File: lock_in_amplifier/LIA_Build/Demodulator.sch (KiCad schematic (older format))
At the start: 0 parts

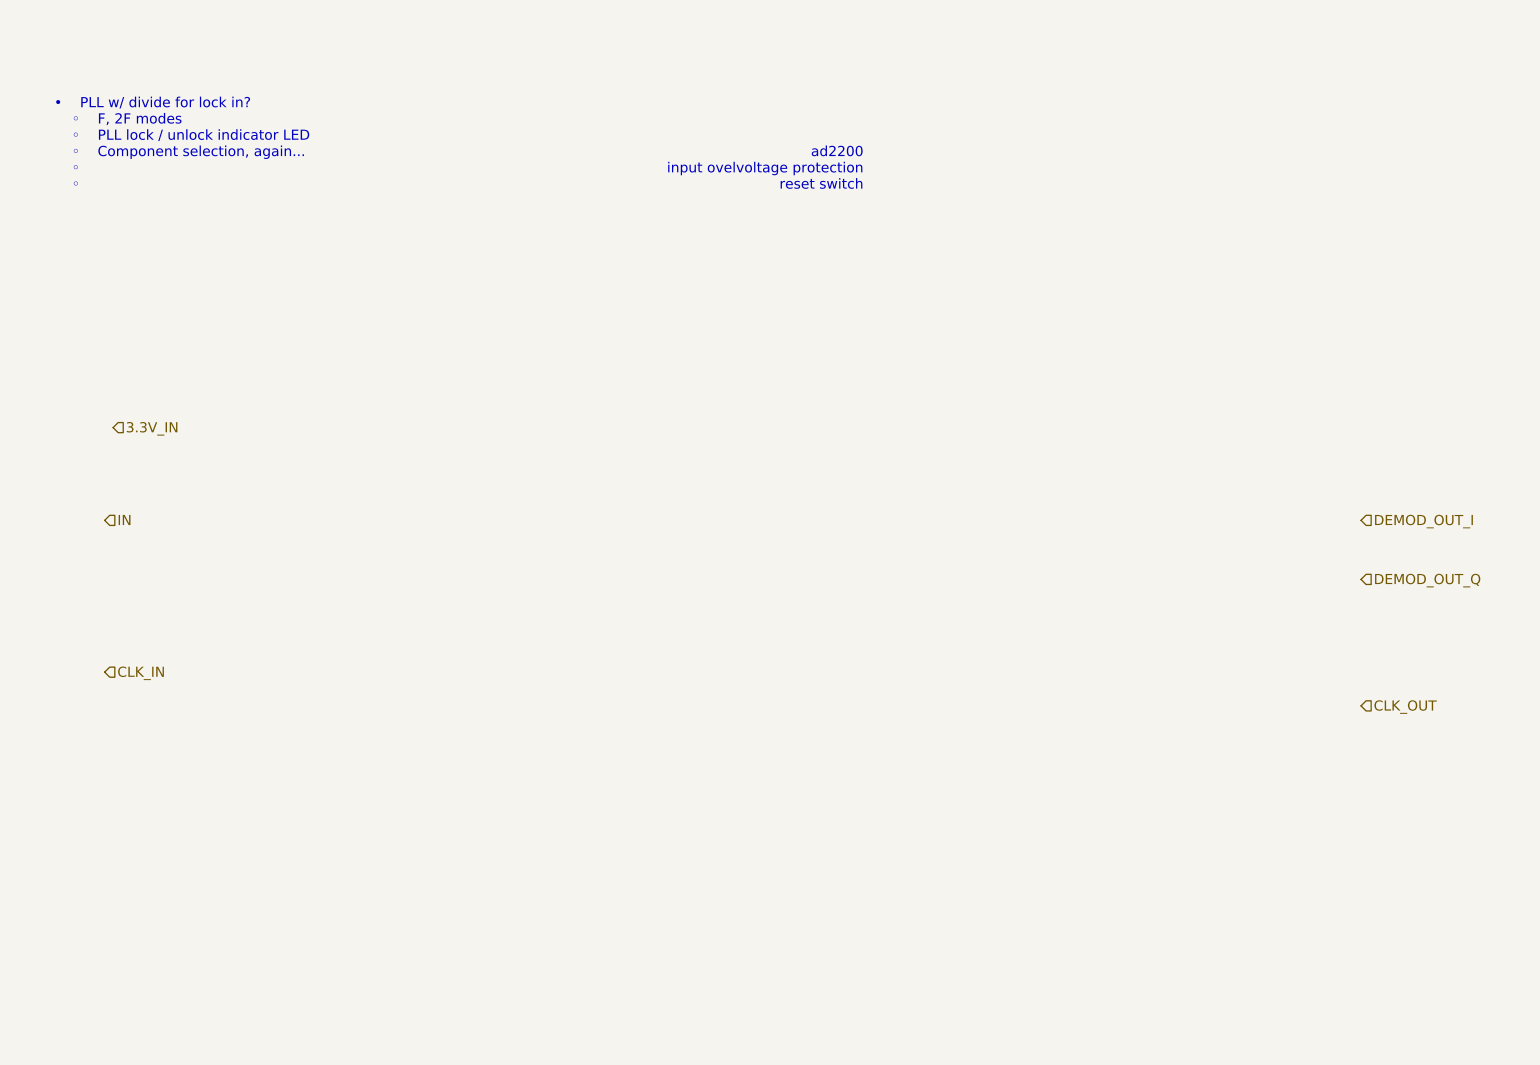
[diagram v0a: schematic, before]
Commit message: power supply, amp chain first pass
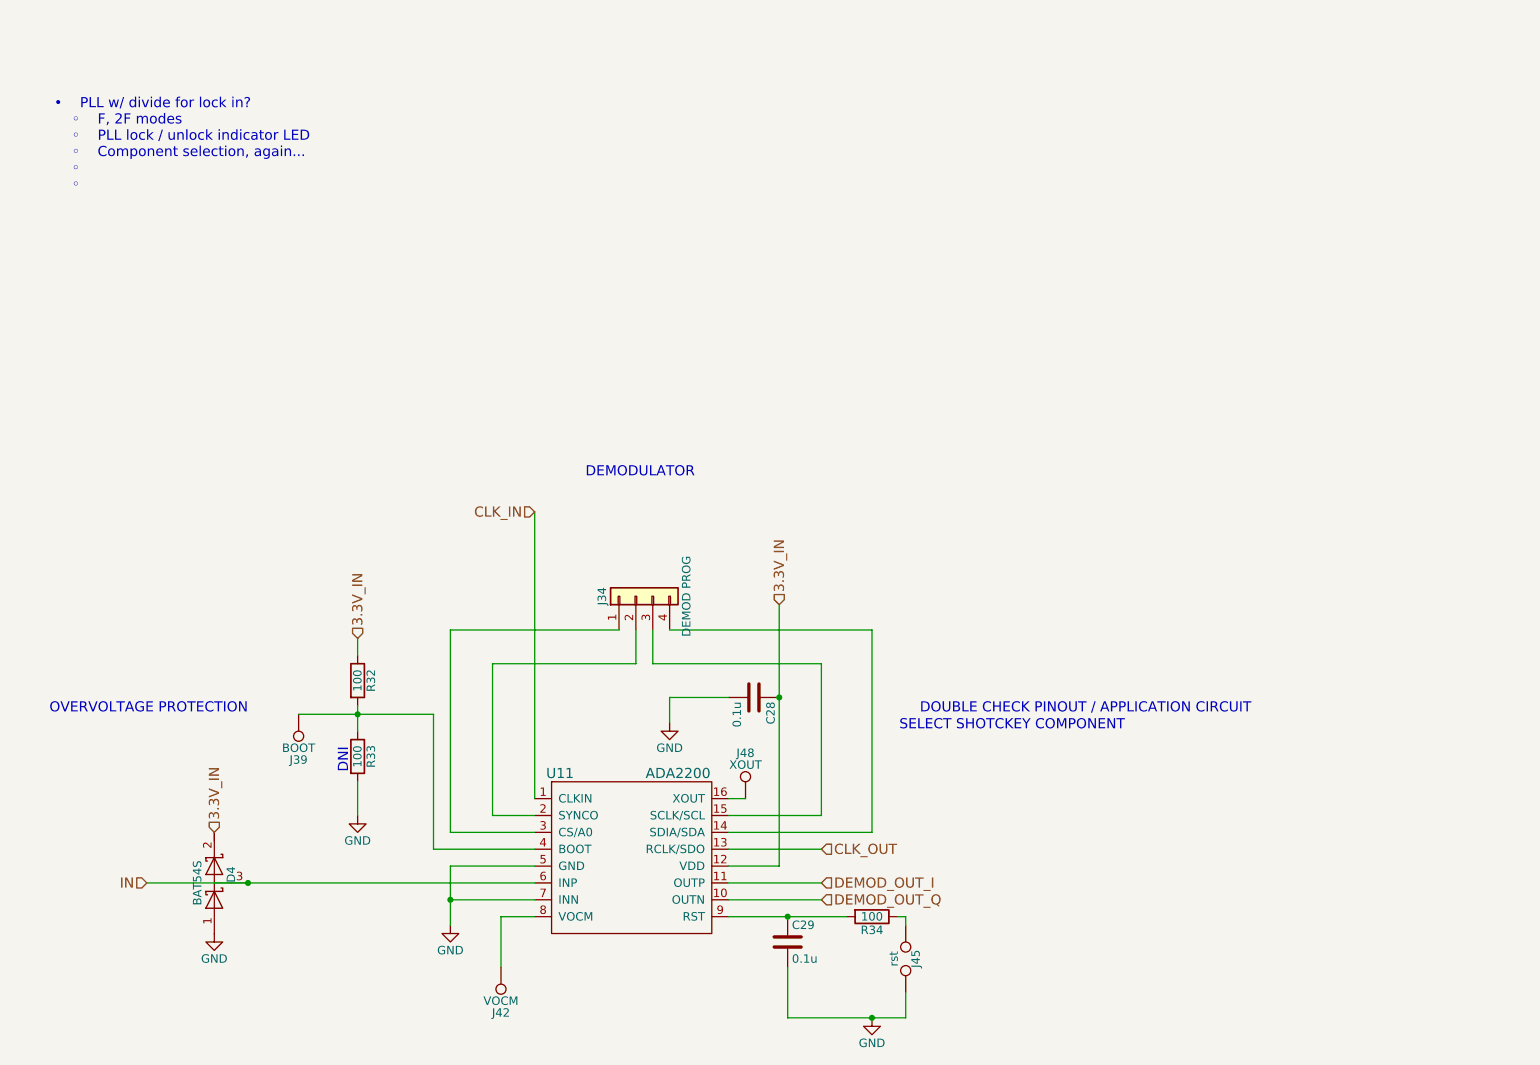
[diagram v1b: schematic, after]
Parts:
- added C28, C29: 0.1u, Capacitors_SMD:C_0805, symbol C
- added D4: BAT54S, TO_SOT_Packages_SMD:SOT-23, symbol D_Schottky_x2_Serial_AKC
- added J34: DEMOD PROG, Pin_Headers:Pin_Header_Straight_1x04_Pitch2.54mm, symbol Conn_01x04
- added J39: BOOT, footprints:tyco_RCU_0603_Probe_Pad, symbol TEST_1P
- added J42: VOCM, footprints:tyco_RCU_0603_Probe_Pad, symbol TEST_1P
- added J45: rst, symbol TEST_2P
- added J48: XOUT, footprints:tyco_RCU_0603_Probe_Pad, symbol TEST_1P
- added R32, R33, R34: 100, Resistors_SMD:R_0805, symbol R
- added U11: ADA2200, Housings_SSOP:TSSOP-20_4.4x6.5mm_Pitch0.65mm, symbol ADA2200
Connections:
- net 3.3V_IN: now also C28.1, D4.2 (K), R32.1, U11.12 (VDD)
- net CLK_IN: now also U11.1 (CLKIN)
- net CLK_OUT: now also U11.13 (RCLK/SDO)
- net DEMOD_OUT_I: now also U11.11 (OUTP)
- net DEMOD_OUT_Q: now also U11.10 (OUTN)
- net IN: now also D4.3 (common), U11.6 (INP)
- new net: J34.4 (Pin_4), U11.14 (SDIA/SDA)
- new net: J34.3 (Pin_3), U11.15 (SCLK/SCL)
- new net: J48.1, U11.16 (XOUT)
- new net: J34.2 (Pin_2), U11.2 (SYNCO)
- new net: J34.1 (Pin_1), U11.3 (CS/A0)
- new net: J39.1, R32.2, R33.1, U11.4 (BOOT)
- new net: J42.1, U11.8 (VOCM)
- new net: C29.1, R34.2, U11.9 (RST)
- new net: J45.1, R34.1
- new net GND: C28.2, C29.2, D4.1 (A), J45.2, R33.2, U11.5 (GND), U11.7 (INN)
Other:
- note added: "DEMODULATOR"
- note added: "DNI"
- note added: "DOUBLE CHECK PINOUT / APPLICATION CIRCUIT"
- note added: "OVERVOLTAGE PROTECTION"
- note added: "SELECT SHOTCKEY COMPONENT"
- note removed: "ad2200\ninput ovelvoltage protection\nreset switch"

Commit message: initial transimpedance selection, lna refinement
amp overload led
switch comps added
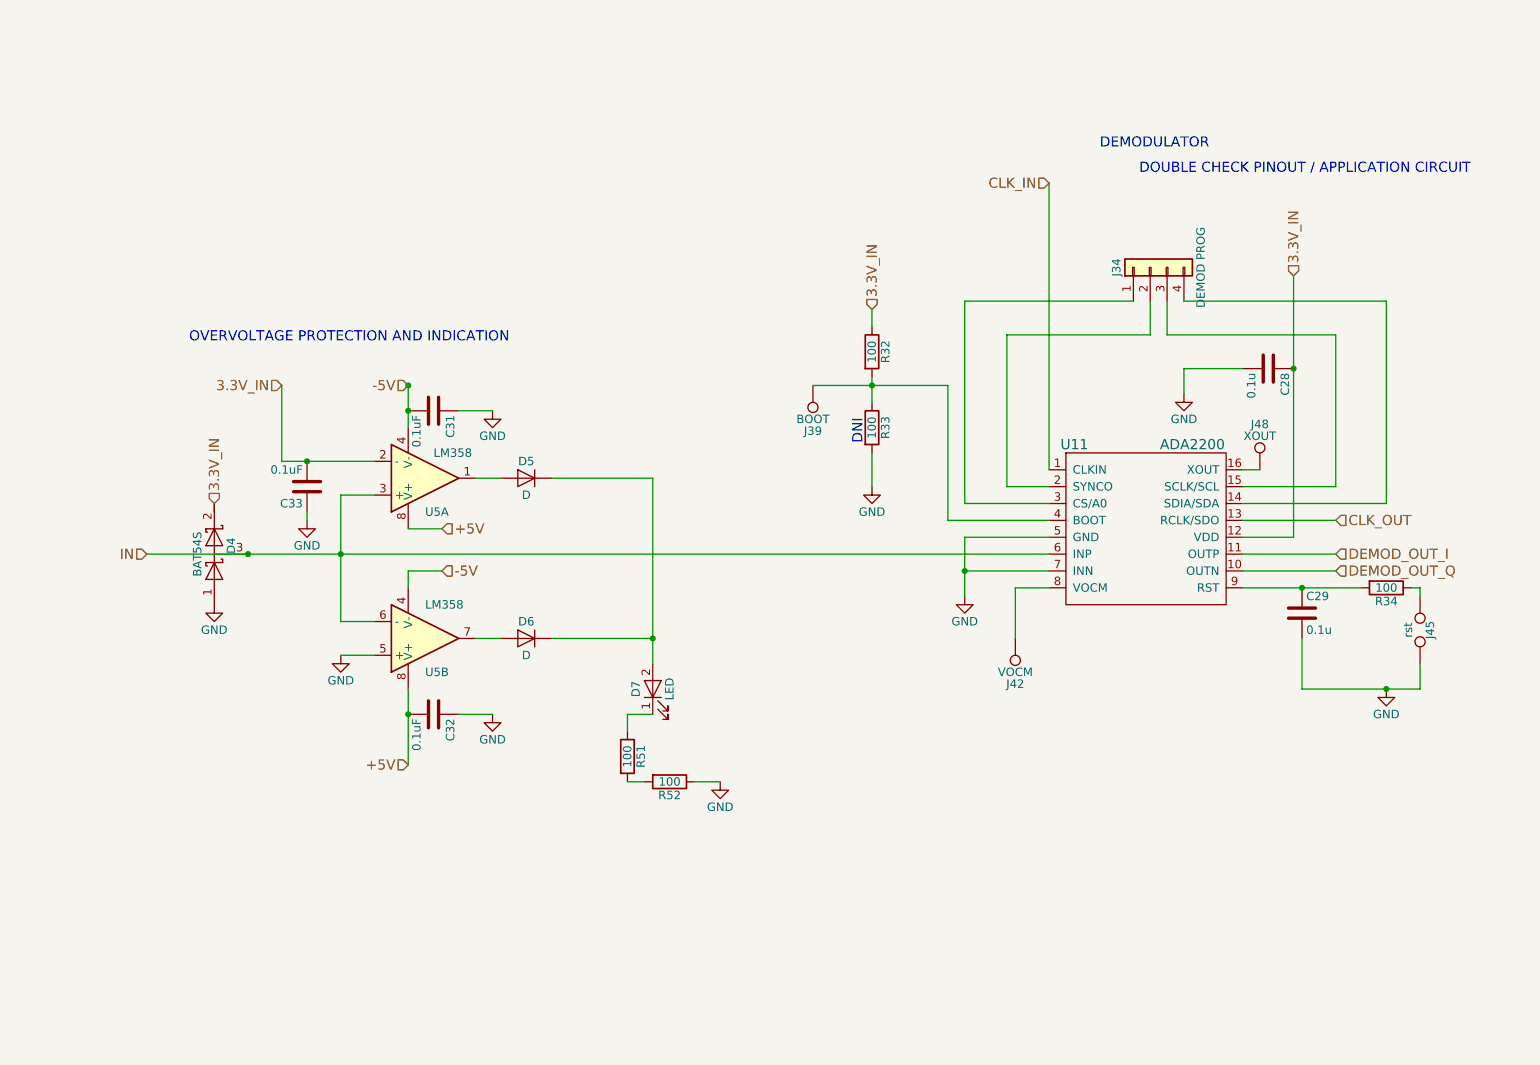
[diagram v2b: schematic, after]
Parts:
- added C31, C32, C33: 0.1uF, symbol C
- added D5, D6: D, symbol D
- added D7: LED, symbol LED
- added R51, R52: 100, symbol R
- added U5: LM358, symbol LM358
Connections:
- net 3.3V_IN: now also C33.2, U5.2 (-)
- net GND: now also C31.1, C32.1, C33.1, R52.1, U5.5 (+)
- net IN: now also U5.3 (+), U5.6 (-)
- new net: D5.2 (A), U5.1
- new net: D6.2 (A), U5.7
- new net: D5.1 (K), D6.1 (K), D7.2 (A)
- new net: D7.1 (K), R51.1
- new net: R51.2, R52.2
- new net +5V: C32.2, U5.8 (V+), U5.8 (V+)
- new net -5V: C31.2, U5.4 (V-), U5.4 (V-)
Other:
- note added: "OVERVOLTAGE PROTECTION AND INDICATION"
- note removed: "OVERVOLTAGE PROTECTION"
- note removed: "SELECT SHOTCKEY COMPONENT"
- note removed: "• PLL w/ divide for lock in?\n ◦ F, 2F modes\n ◦ PLL lock / unlock indicator LED\n ◦ Component selection, again...\n ◦ \n ◦ \n"
- moved on the sheet: C28, C29, D4, J34, J39, J42, J45, J48, R32, R33, R34, U11

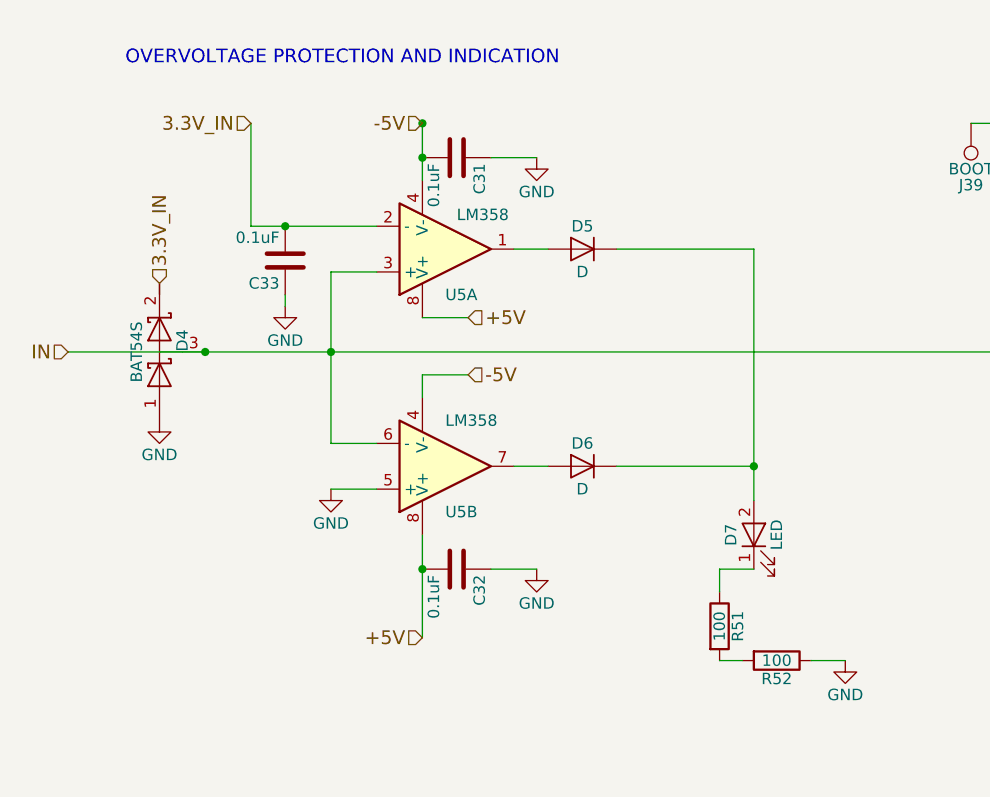
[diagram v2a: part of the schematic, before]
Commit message: switch footprints, lm833 usage, pll investigation
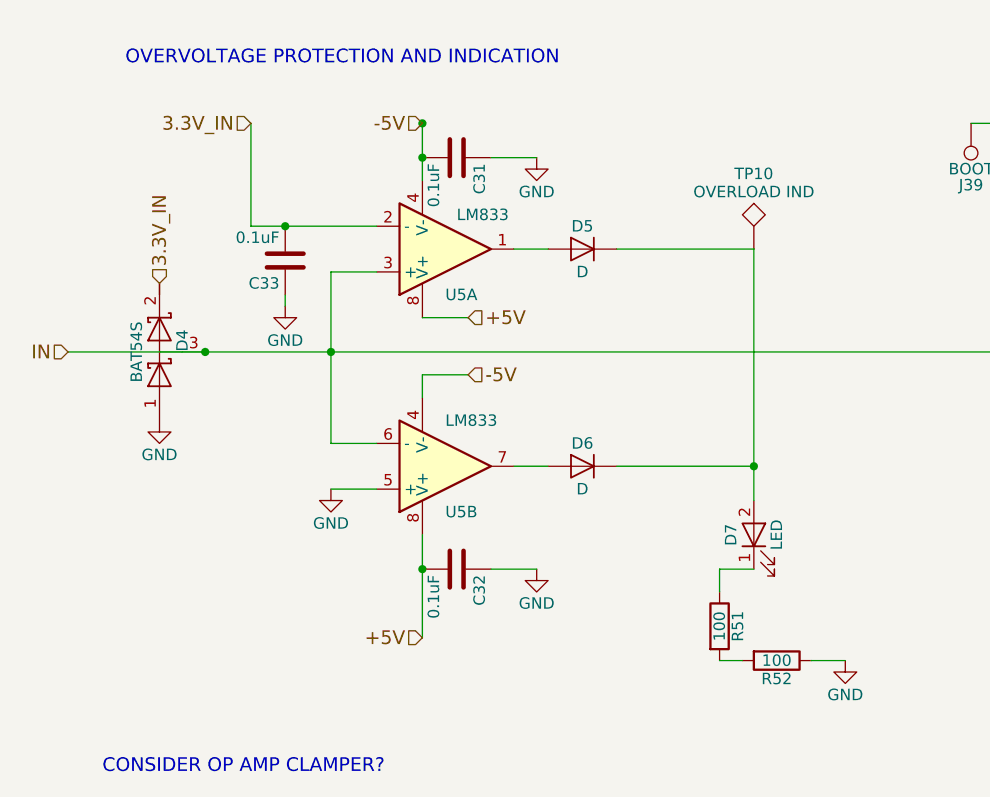
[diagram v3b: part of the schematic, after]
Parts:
- added TP10: OVERLOAD IND, symbol TEST
- U5: value LM358 -> LM833
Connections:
- net at D5.1 (K), D6.1 (K), D7.2 (A): now also TP10.1
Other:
- note added: "CONSIDER OP AMP CLAMPER?"
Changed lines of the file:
@@
 P 2950 3500
 F 0 "U5" H 2950 3700 50  0000 L CNN
-F 1 "LM358" H 3000 3350 50  0000 L CNN
+F 1 "LM833" H 3000 3350 50  0000 L CNN
 F 2 "" H 2950 3500 50  0001 C CNN
 F 3 "" H 2950 3500 50  0001 C CNN
@@
 P 2950 4450
 F 0 "U5" H 2950 4650 50  0000 L CNN
-F 1 "LM358" H 2950 4250 50  0000 L CNN
+F 1 "LM833" H 2950 4250 50  0000 L CNN
 F 2 "" H 2950 4450 50  0001 C CNN
 F 3 "" H 2950 4450 50  0001 C CNN
@@
 	2100 2950 2100 3400
 Connection ~ 2250 3400
+$Comp
+L TEST TP10
+U 1 1 5A23FBD3
+P 4300 3500
+F 0 "TP10" H 4300 3800 50  0000 C BNN
+F 1 "OVERLOAD IND" H 4300 3750 50  0000 C CNN
+F 2 "" H 4300 3500 50  0001 C CNN
+F 3 "" H 4300 3500 50  0001 C CNN
+	1    4300 3500
+	1    0    0    -1
+$EndComp
+Text Notes 1450 5800 0    60   ~ 0
+CONSIDER OP AMP CLAMPER?
 $EndSCHEMATC
